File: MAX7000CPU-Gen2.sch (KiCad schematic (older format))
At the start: 131 parts, among them J1 Conn_01x08_Male, J2 Conn_01x08_Male, J3 Conn_01x08_Male, J4 Conn_02x05_Odd_Even, J5 Conn_01x05_Male, SW1 SW_Push, SW2 SW_Push, SW3 SW_Push, U1 NE555P, U10 74LS241, U11 74LS241, U12 74LS241, U13 CD4029BEE4, U14 CD4029BEE4, U15 74LS574, U16 74LS241, U17 CD4029BEE4, U18 CD4029BEE4, U19 AS6C1008-55PCN, U2 NE555P, U20 74LS241, U21 74LS574, U22 CD4029BEE4, U23 CD4029BEE4, U24 74LS241, U25 74LS574, U26 74LS574, U27 74LS574, U28 CD4029BEE4, U3 NE555P, U4 74LS574, U5 74LS574, U6 74LS574, U7 CD4029BEE4, U8 EPM7128slc84-15n, U9 74LS574

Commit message: silk screening - clock module
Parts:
- renumbered C6 to C1, C5 to C2, C4 to C3, C3 to C4, C2 to C5, C1 to C6, R6 to R1, R1 to R2, R5 to R3, R3 to R4, R4 to R5, R2 to R6, SW2 to SW1, SW1 to SW2, U2 to U1, U3 to U2, U1 to U3
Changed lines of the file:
@@
 	1000 1400 1000 1900
 $Comp
-L MAX7000CPU-Gen2-rescue:C-Device C5
+L MAX7000CPU-Gen2-rescue:C-Device C2
 U 1 1 60EC4E13
 P 1000 2050
-F 0 "C5" H 750 2100 50  0000 L CNN
+F 0 "C2" H 750 2100 50  0000 L CNN
 F 1 "10n" H 650 2000 50  0000 L CNN
 F 2 "Capacitor_THT:C_Disc_D5.0mm_W2.5mm_P2.50mm" H 1038 1900 50  0001 C CNN
@@
 $EndComp
 $Comp
-L MAX7000CPU-Gen2-rescue:C-Device C6
+L MAX7000CPU-Gen2-rescue:C-Device C1
 U 1 1 60EC5A74
 P 1300 2050
-F 0 "C6" H 1415 2096 50  0000 L CNN
+F 0 "C1" H 1415 2096 50  0000 L CNN
 F 1 "10n" H 1415 2005 50  0000 L CNN
 F 2 "Capacitor_THT:C_Disc_D5.0mm_W2.5mm_P2.50mm" H 1338 1900 50  0001 C CNN
@@
 	1300 1850 2050 1850
 $Comp
-L MAX7000CPU-Gen2-rescue:R-Device R1
+L MAX7000CPU-Gen2-rescue:R-Device R2
 U 1 1 60EC8EAA
 P 2300 950
-F 0 "R1" H 2370 996 50  0000 L CNN
+F 0 "R2" H 2370 996 50  0000 L CNN
 F 1 "1K" H 2370 905 50  0000 L CNN
 F 2 "Resistor_THT:R_Axial_DIN0207_L6.3mm_D2.5mm_P7.62mm_Horizontal" V 2230 950 50  0001 C CNN
@@
 	2300 1400 2300 1100
 $Comp
-L MAX7000CPU-Gen2-rescue:R-Device R6
+L MAX7000CPU-Gen2-rescue:R-Device R1
 U 1 1 60ECC1C1
 P 2200 1850
-F 0 "R6" V 1993 1850 50  0000 C CNN
+F 0 "R1" V 1993 1850 50  0000 C CNN
 F 1 "1K" V 2084 1850 50  0000 C CNN
 F 2 "Resistor_THT:R_Axial_DIN0207_L6.3mm_D2.5mm_P7.62mm_Horizontal" V 2130 1850 50  0001 C CNN
@@
 $EndComp
 $Comp
-L MAX7000CPU-Gen2-rescue:NE555P-Timer U3
+L MAX7000CPU-Gen2-rescue:NE555P-Timer U2
 U 1 1 60ED5104
 P 3800 1400
-F 0 "U3" H 3450 1850 50  0000 C CNN
+F 0 "U2" H 3450 1850 50  0000 C CNN
 F 1 "NE555P" H 3550 1750 50  0000 C CNN
 F 2 "Package_DIP:DIP-8_W7.62mm" H 4450 1000 50  0001 C CNN
@@
 $EndComp
 $Comp
-L MAX7000CPU-Gen2-rescue:R-Device R3
+L MAX7000CPU-Gen2-rescue:R-Device R4
 U 1 1 60ED71C4
 P 4400 1000
-F 0 "R3" H 4470 1046 50  0000 L CNN
+F 0 "R4" H 4470 1046 50  0000 L CNN
 F 1 "1M" H 4470 955 50  0000 L CNN
 F 2 "Resistor_THT:R_Axial_DIN0207_L6.3mm_D2.5mm_P7.62mm_Horizontal" V 4330 1000 50  0001 C CNN
@@
 $EndComp
 $Comp
-L MAX7000CPU-Gen2-rescue:R-Device R5
+L MAX7000CPU-Gen2-rescue:R-Device R3
 U 1 1 60ED8890
 P 3150 1050
-F 0 "R5" H 3000 1150 50  0000 L CNN
+F 0 "R3" H 3000 1150 50  0000 L CNN
 F 1 "1K" H 3000 1050 50  0000 L CNN
 F 2 "Resistor_THT:R_Axial_DIN0207_L6.3mm_D2.5mm_P7.62mm_Horizontal" V 3080 1050 50  0001 C CNN
@@
 $EndComp
 $Comp
-L MAX7000CPU-Gen2-rescue:C-Device C4
+L MAX7000CPU-Gen2-rescue:C-Device C3
 U 1 1 60ED8E14
 P 4400 1850
-F 0 "C4" H 4515 1896 50  0000 L CNN
+F 0 "C3" H 4515 1896 50  0000 L CNN
 F 1 "100n" H 4515 1805 50  0000 L CNN
 F 2 "Capacitor_THT:C_Disc_D5.0mm_W2.5mm_P2.50mm" H 4438 1700 50  0001 C CNN
@@
 $EndComp
 $Comp
-L MAX7000CPU-Gen2-rescue:C-Device C3
+L MAX7000CPU-Gen2-rescue:C-Device C4
 U 1 1 60ED989B
 P 3150 1850
-F 0 "C3" H 3265 1896 50  0000 L CNN
+F 0 "C4" H 3265 1896 50  0000 L CNN
 F 1 "10n" H 3265 1805 50  0000 L CNN
 F 2 "Capacitor_THT:C_Disc_D5.0mm_W2.5mm_P2.50mm" H 3188 1700 50  0001 C CNN
@@
 	3800 2000 3150 2000
 $Comp
-L MAX7000CPU-Gen2-rescue:SW_Push-Switch SW2
+L MAX7000CPU-Gen2-rescue:SW_Push-Switch SW1
 U 1 1 60EDF059
 P 2950 1200
-F 0 "SW2" H 2750 1300 50  0000 C CNN
+F 0 "SW1" H 2750 1300 50  0000 C CNN
 F 1 "SW_Push" H 2950 1150 50  0000 C CNN
 F 2 "Button_Switch_THT:SW_PUSH_6mm" H 2950 1400 50  0001 C CNN
@@
 $EndComp
 $Comp
-L power:+5V #PWR035
+L MAX7000CPU-Gen2-rescue:+5V-power #PWR035
 U 1 1 61298F38
 P 4100 4800
@@
 $EndComp
 $Comp
-L power:+5V #PWR048
+L MAX7000CPU-Gen2-rescue:+5V-power #PWR048
 U 1 1 612A2499
 P 4050 6900
@@
 $EndComp
 $Comp
-L power:+5V #PWR059
+L MAX7000CPU-Gen2-rescue:+5V-power #PWR059
 U 1 1 6165CC62
 P 1400 8850
@@
 $EndComp
 $Comp
-L power:+5V #PWR056
+L MAX7000CPU-Gen2-rescue:+5V-power #PWR056
 U 1 1 61A5F3D6
 P 8600 8500
@@
 $EndComp
 $Comp
-L power:+5V #PWR055
+L MAX7000CPU-Gen2-rescue:+5V-power #PWR055
 U 1 1 61D0102F
 P 4450 7850
@@
 Connection ~ 5200 1150
 $Comp
-L MAX7000CPU-Gen2-rescue:SW_Push-Switch SW1
+L MAX7000CPU-Gen2-rescue:SW_Push-Switch SW2
 U 1 1 60EEC6A4
 P 5000 1150
-F 0 "SW1" H 4800 1250 50  0000 C CNN
+F 0 "SW2" H 4800 1250 50  0000 C CNN
 F 1 "SW_Push" H 5000 1100 50  0000 C CNN
 F 2 "Button_Switch_THT:SW_PUSH_6mm" H 5000 1350 50  0001 C CNN
@@
 	6450 1100 6450 1350
 $Comp
-L MAX7000CPU-Gen2-rescue:C-Device C1
+L MAX7000CPU-Gen2-rescue:C-Device C6
 U 1 1 60EEC68A
 P 5200 1800
-F 0 "C1" H 5315 1846 50  0000 L CNN
+F 0 "C6" H 5315 1846 50  0000 L CNN
 F 1 "10n" H 5315 1755 50  0000 L CNN
 F 2 "Capacitor_THT:C_Disc_D5.0mm_W2.5mm_P2.50mm" H 5238 1650 50  0001 C CNN
@@
 $EndComp
 $Comp
-L MAX7000CPU-Gen2-rescue:C-Device C2
+L MAX7000CPU-Gen2-rescue:C-Device C5
 U 1 1 60EEC684
 P 6450 1800
-F 0 "C2" H 6565 1846 50  0000 L CNN
+F 0 "C5" H 6565 1846 50  0000 L CNN
 F 1 "100n" H 6565 1755 50  0000 L CNN
 F 2 "Capacitor_THT:C_Disc_D5.0mm_W2.5mm_P2.50mm" H 6488 1650 50  0001 C CNN
@@
 $EndComp
 $Comp
-L MAX7000CPU-Gen2-rescue:R-Device R4
+L MAX7000CPU-Gen2-rescue:R-Device R5
 U 1 1 60EEC67E
 P 5200 1000
-F 0 "R4" H 5050 1100 50  0000 L CNN
+F 0 "R5" H 5050 1100 50  0000 L CNN
 F 1 "1K" H 5050 1000 50  0000 L CNN
 F 2 "Resistor_THT:R_Axial_DIN0207_L6.3mm_D2.5mm_P7.62mm_Horizontal" V 5130 1000 50  0001 C CNN
@@
 $EndComp
 $Comp
-L MAX7000CPU-Gen2-rescue:R-Device R2
+L MAX7000CPU-Gen2-rescue:R-Device R6
 U 1 1 60EEC678
 P 6450 950
-F 0 "R2" H 6520 996 50  0000 L CNN
+F 0 "R6" H 6520 996 50  0000 L CNN
 F 1 "1M" H 6520 905 50  0000 L CNN
 F 2 "Resistor_THT:R_Axial_DIN0207_L6.3mm_D2.5mm_P7.62mm_Horizontal" V 6380 950 50  0001 C CNN
@@
 $EndComp
 $Comp
-L MAX7000CPU-Gen2-rescue:NE555P-Timer U1
+L MAX7000CPU-Gen2-rescue:NE555P-Timer U3
 U 1 1 60EEC672
 P 5850 1350
-F 0 "U1" H 5500 1800 50  0000 C CNN
+F 0 "U3" H 5500 1800 50  0000 C CNN
 F 1 "NE555P" H 5600 1700 50  0000 C CNN
 F 2 "Package_DIP:DIP-8_W7.62mm" H 6500 950 50  0001 C CNN
@@
 $EndComp
 $Comp
-L MAX7000CPU-Gen2-rescue:NE555P-Timer U2
+L MAX7000CPU-Gen2-rescue:NE555P-Timer U1
 U 1 1 60EBAC9F
 P 1550 1400
-F 0 "U2" H 1200 1850 50  0000 C CNN
+F 0 "U1" H 1200 1850 50  0000 C CNN
 F 1 "NE555P" H 1300 1750 50  0000 C CNN
 F 2 "Package_DIP:DIP-8_W7.62mm" H 2200 1000 50  0001 C CNN
@@
 	3700 5650 3700 6700
 $Comp
-L power:+5V #PWR0101
+L MAX7000CPU-Gen2-rescue:+5V-power #PWR0101
 U 1 1 614B9F5E
 P 3650 6100
@@
 $EndComp
 $Comp
-L power:+5V #PWR0102
+L MAX7000CPU-Gen2-rescue:+5V-power #PWR0102
 U 1 1 614BAC35
 P 3700 3900

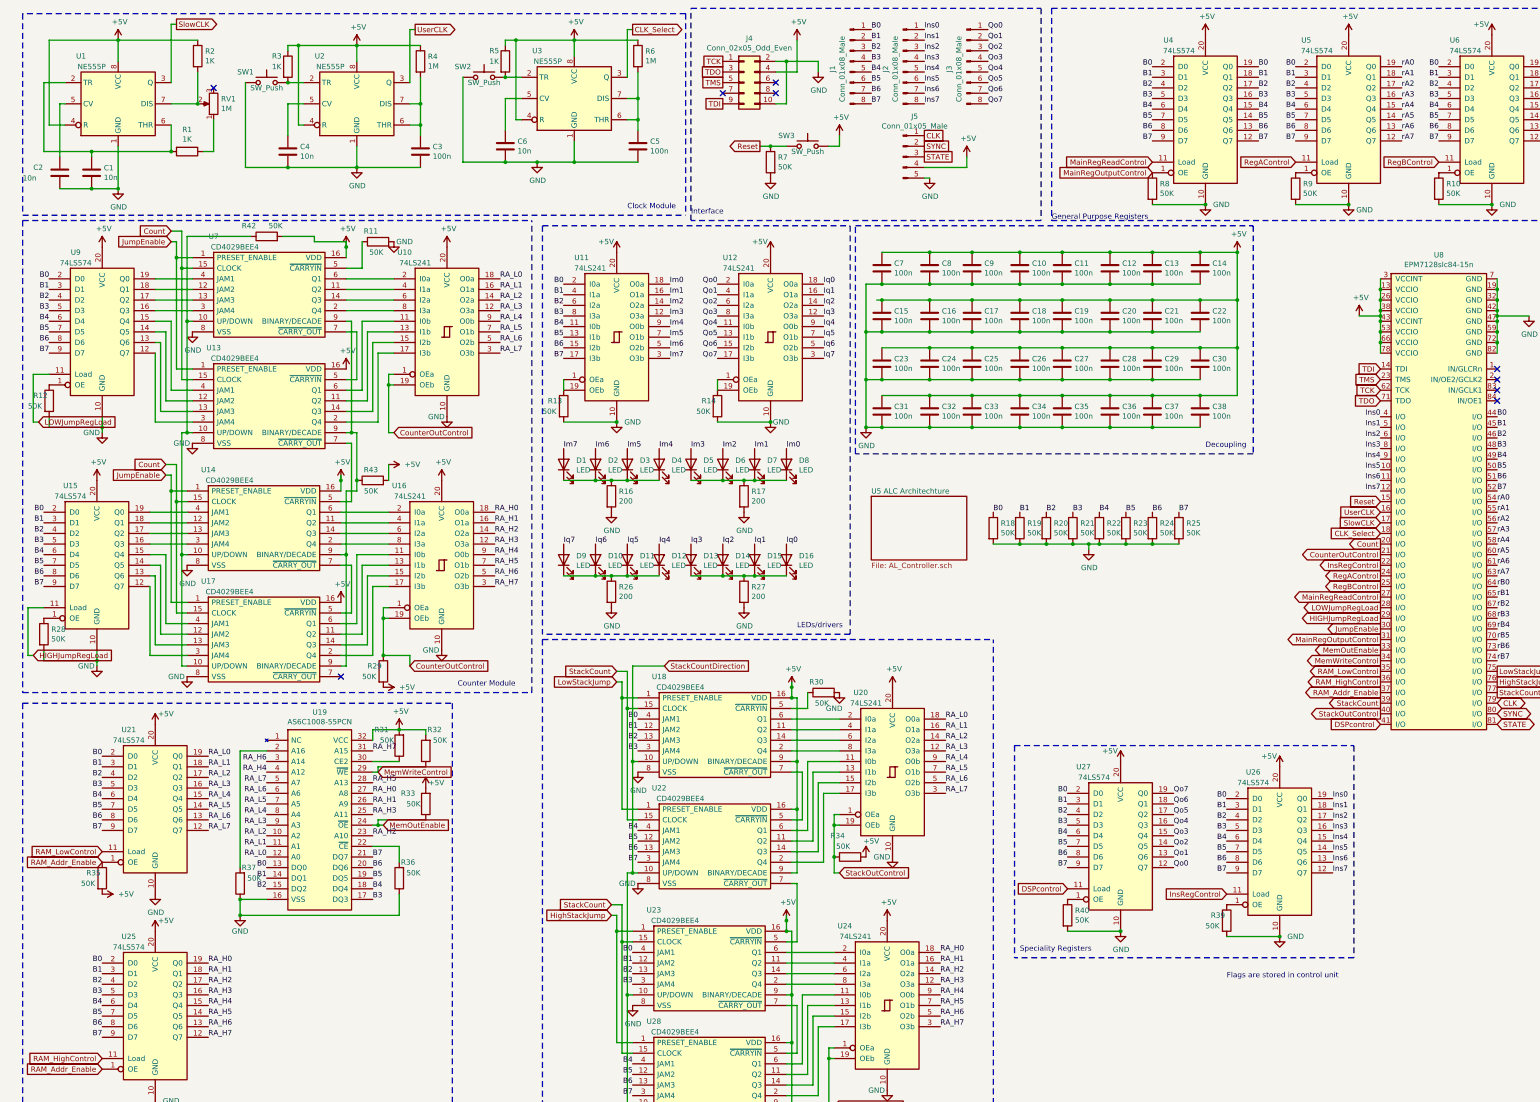
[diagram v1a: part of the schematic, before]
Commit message: silkscreening and 3d models implemented
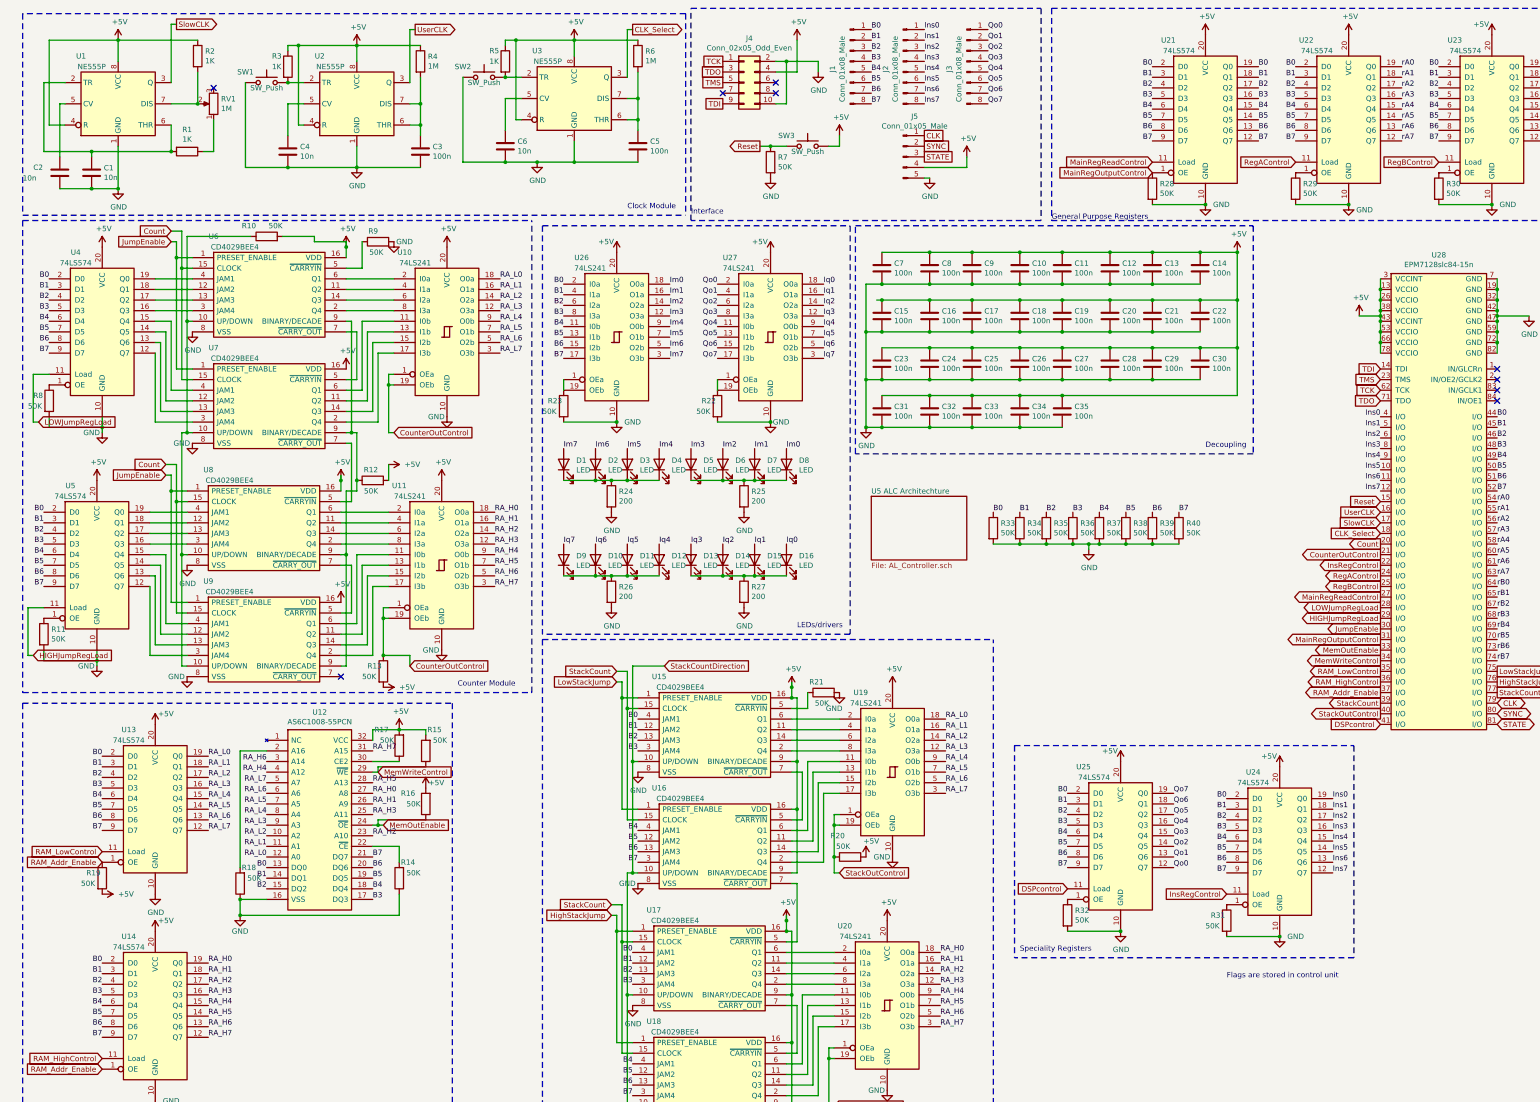
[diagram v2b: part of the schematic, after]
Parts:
- removed C36, C37, C38: 100n, Capacitor_SMD:C_0805_2012Metric_Pad1.18x1.45mm_HandSolder, symbol MAX7000CPU-Gen2-rescue:C-Device
- renumbered R42 to R10, R28 to R11, R43 to R12, R29 to R13, R36 to R14, R32 to R15, R33 to R16, R31 to R17, R37 to R18, R35 to R19, R34 to R20, R30 to R21, R14 to R22, R13 to R23, R16 to R24, R17 to R25, R8 to R28, R9 to R29, R10 to R30, R39 to R31, R40 to R32, R18 to R33, R19 to R34, R20 to R35, R21 to R36, R22 to R37, R23 to R38, R24 to R39, R25 to R40, R12 to R8, R11 to R9, U16 to U11, U19 to U12, U21 to U13, U25 to U14, U18 to U15, U22 to U16, U23 to U17, U28 to U18, U20 to U19, U24 to U20, U4 to U21, U5 to U22, U6 to U23, U26 to U24, U27 to U25, U11 to U26, U12 to U27, U8 to U28, U9 to U4, U15 to U5, U7 to U6, U13 to U7, U14 to U8, U17 to U9

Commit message: controller timing
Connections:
- net DSPcontrol renamed DisplayControl
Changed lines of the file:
@@
 B7
 Text GLabel 10500 8800 0    50   Input ~ 0
-DSPcontrol
+DisplayControl
 Text Notes 10050 9400 0    50   ~ 0
 Speciality Registers
@@
 Flags are stored in control unit
 Text GLabel 13450 7250 0    50   Input ~ 0
-DSPcontrol
+DisplayControl
 Text GLabel 14550 7050 2    50   BiDi ~ 0
 CLK
@@
 	3800 4950 3800 5050
 Wire Notes Line
-	10000 7450 13200 7450
-Wire Notes Line
 	13200 7450 13200 9450
 Wire Notes Line
-	13200 9450 10000 9450
-Wire Notes Line
-	10000 7450 10000 9450
+	9900 7450 9900 9450
 Wire Wire Line
 	8250 10400 8250 10850
@@
 Wire Wire Line
 	10450 4150 12100 4150
+Wire Notes Line
+	9900 7450 13200 7450
+Wire Notes Line
+	9900 9450 13200 9450
 $EndSCHEMATC

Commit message: Basic Jumps Working + RepoCleaning
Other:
- note added: "Main RegOutput Should probs be pulled high!!!\nCounterOutControlShould be pulled Low\nOutput Register is configured backwards\n\n"
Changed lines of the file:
@@
 Wire Notes Line
 	9900 9450 13200 9450
+Text Notes 10250 350  0    50   ~ 0
+Main RegOutput Should probs be pulled high!!!\nCounterOutControlShould be pulled Low\nOutput Register is configured backwards\n\n
 $EndSCHEMATC
